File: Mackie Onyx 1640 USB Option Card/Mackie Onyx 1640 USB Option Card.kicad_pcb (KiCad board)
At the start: 2 copper layers, 193 x 90 mm, 7 parts, among them J1 Conn_02x17_Odd_Even, U1 XU316-1024-QF60B-C24, U2 CS5368-CQZ, U3 CS5368-CQZ, U4 CS5368-CQZ

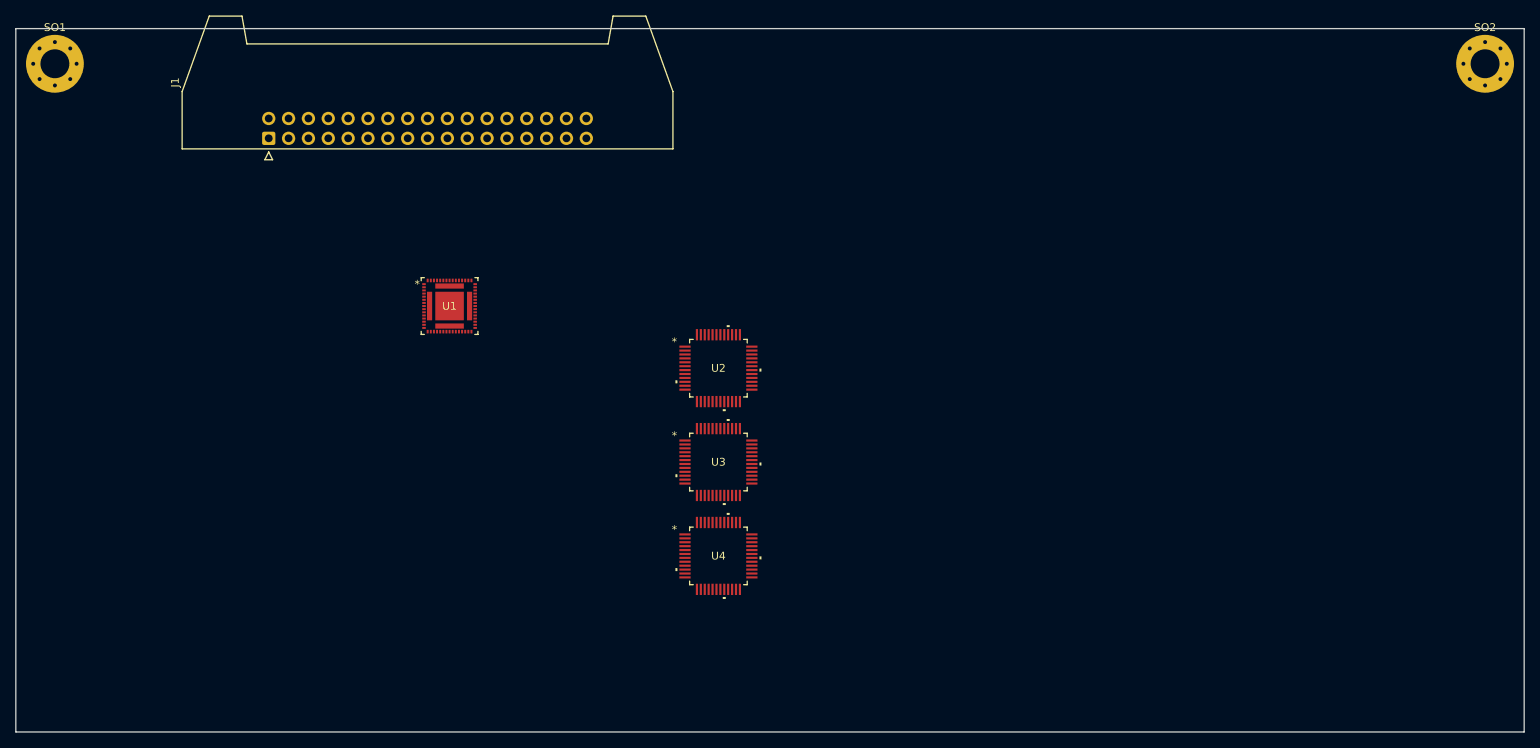
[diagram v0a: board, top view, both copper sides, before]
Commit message: Added a TI-TLV320 ADC Added power for ADC put the filter caps next to pins where they belong Added footprints for ADC and MCU
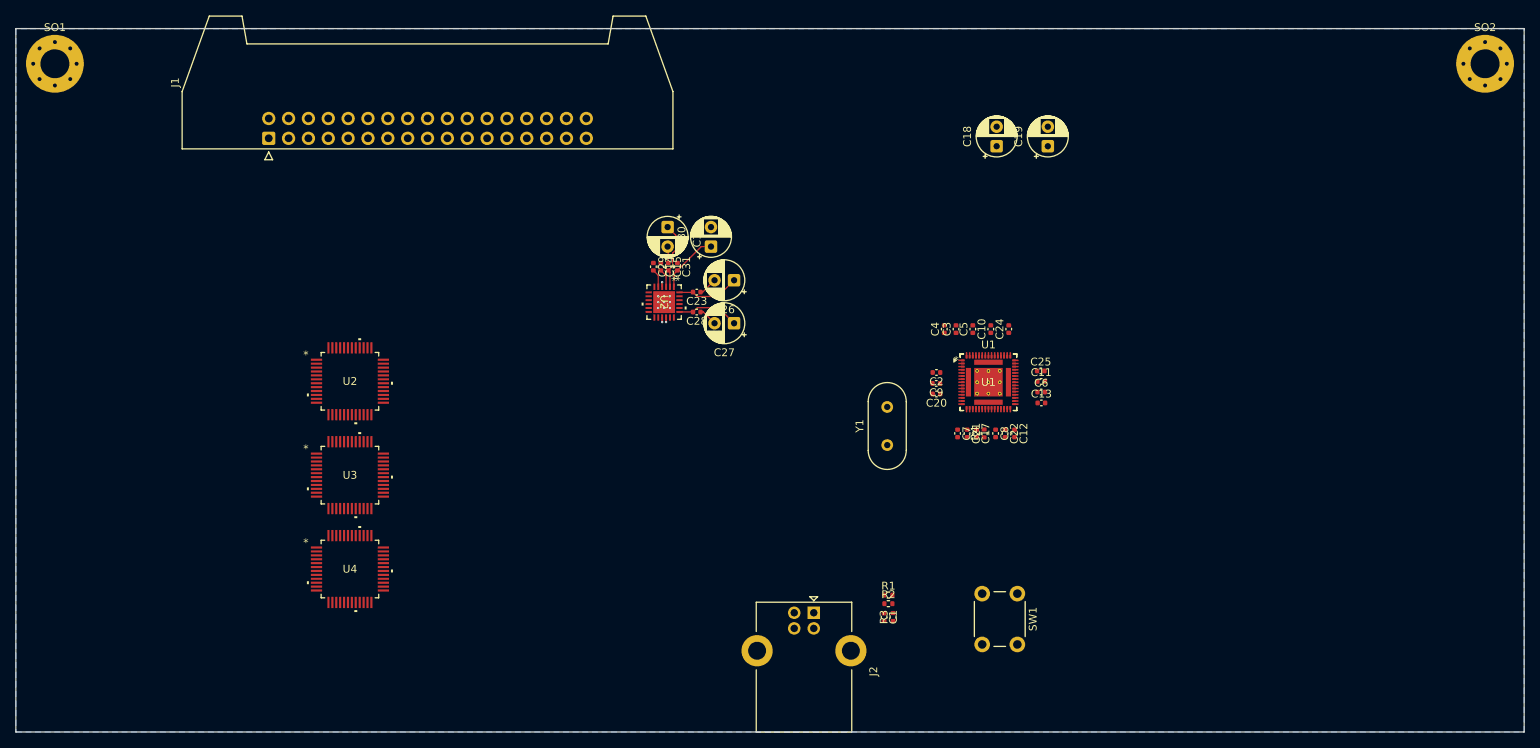
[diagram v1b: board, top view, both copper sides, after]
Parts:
- added C1: 2u2C, Capacitor_SMD:C_0402_1005Metric, F.Cu at (161.1, 125.3)
- added C10: 100nC, Capacitor_SMD:C_0402_1005Metric, F.Cu at (174.8, 88.5)
- added C11: 100nC, Capacitor_SMD:C_0402_1005Metric, F.Cu at (181.2, 95.2)
- added C12: 100nC, Capacitor_SMD:C_0402_1005Metric, F.Cu at (177.8, 101.8)
- added C13: 100nC, Capacitor_SMD:C_0402_1005Metric, F.Cu at (181.2, 97.9)
- added C14: 1uC, Capacitor_SMD:C_0402_1005Metric, F.Cu at (132.5, 80.5)
- added C15: 100nC, Capacitor_SMD:C_0402_1005Metric, F.Cu at (133.5, 80.5)
- added C16: 10uC_Polarized, Capacitor_THT:CP_Radial_D5.0mm_P2.50mm, F.Cu at (133.4, 75.4)
- added C17: 1uC, Capacitor_SMD:C_0402_1005Metric, F.Cu at (172.9, 101.8)
- added C18: 10uC_Polarized, Capacitor_THT:CP_Radial_D5.0mm_P2.50mm, F.Cu at (175.5, 65.0)
- added C19: 10uC_Polarized, Capacitor_THT:CP_Radial_D5.0mm_P2.50mm, F.Cu at (182.1, 65.0)
- added C2: 100nC, Capacitor_SMD:C_0402_1005Metric, F.Cu at (167.8, 94.0)
- added C20: 100nC, Capacitor_SMD:C_0402_1005Metric, F.Cu at (167.8, 96.8)
- added C21: 100nC, Capacitor_SMD:C_0402_1005Metric, F.Cu at (171.7, 101.8)
- added C22: 100nC, Capacitor_SMD:C_0402_1005Metric, F.Cu at (176.6, 101.8)
- added C23: 100nC, Capacitor_SMD:C_0402_1005Metric, F.Cu at (137.1, 83.7)
- added C24: 100nC, Capacitor_SMD:C_0402_1005Metric, F.Cu at (177.1, 88.5)
- added C25: 100nC, Capacitor_SMD:C_0402_1005Metric, F.Cu at (181.2, 93.8)
- added C26: 10uC_Polarized, Capacitor_THT:CP_Radial_D5.0mm_P2.50mm, F.Cu at (141.9, 82.2)
- added C27: 10uC_Polarized, Capacitor_THT:CP_Radial_D5.0mm_P2.50mm, F.Cu at (141.9, 87.7)
- added C28: 100nC, Capacitor_SMD:C_0402_1005Metric, F.Cu at (137.1, 86.3)
- added C29: 1uC, Capacitor_SMD:C_0402_1005Metric, F.Cu at (131.6, 80.5)
- added C3: 100nC, Capacitor_SMD:C_0402_1005Metric, F.Cu at (170.3, 88.5)
- added C30: 10uC_Polarized, Capacitor_THT:CP_Radial_D5.0mm_P2.50mm, F.Cu at (138.9, 77.9)
- added C31: 100nC, Capacitor_SMD:C_0402_1005Metric, F.Cu at (134.7, 80.5)
- added C4: 100nC, Capacitor_SMD:C_0402_1005Metric, F.Cu at (168.8, 88.5)
- added C5: 100nC, Capacitor_SMD:C_0402_1005Metric, F.Cu at (172.4, 88.5)
- added C6: 100nC, Capacitor_SMD:C_0402_1005Metric, F.Cu at (181.2, 96.5)
- added C7: 100nC, Capacitor_SMD:C_0402_1005Metric, F.Cu at (170.5, 101.8)
- added C8: 100nC, Capacitor_SMD:C_0402_1005Metric, F.Cu at (175.4, 101.8)
- added C9: 100nC, Capacitor_SMD:C_0402_1005Metric, F.Cu at (167.8, 95.4)
- added J2: USB_B, Connector_USB:USB_B_Lumberg_2411_02_Horizontal, F.Cu at (152.1, 124.7)
- added R1: 47kR, Resistor_SMD:R_0402_1005Metric, F.Cu at (161.7, 122.5)
- added R2: 220kR, Resistor_SMD:R_0402_1005Metric, F.Cu at (161.7, 123.6)
- added R3: 330kR, Resistor_SMD:R_0402_1005Metric, F.Cu at (162.2, 125.3)
- added R4: 600R@100Mhz, Resistor_SMD:R_0402_1005Metric, F.Cu at (173.9, 101.8)
- added SW1: SW_Push, Button_Switch_THT:SW_PUSH_6mm, F.Cu at (178.2, 122.3)
- added U1: XU316-1024-QF60B-C24, Package_DFN_QFN:QFN-60-1EP_7x7mm_P0.4mm_EP3.4x3.4mm_ThermalVias, F.Cu at (174.4, 95.2)
- added U2: TLV320ADC5140IRTWR, Mackie Onyx 1640 USB Option Card:RTW24_4P15X4P15_TEX, F.Cu at (132.9, 85.0)
- added Y1: 24MHz Crystal, Crystal:Crystal_HC49-U_Vertical, F.Cu at (161.5, 103.3)
- moved U1 69.6 mm to (174.4, 95.2)
- moved U2 47.2 mm to (92.8, 95.1)
- moved U3 47.2 mm to (92.8, 107.1)
- moved U4 47.2 mm to (92.8, 119.2)
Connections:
- J1 pad 1: unconnected-(J1-Pin_1-Pad1) -> /Connector/CH1
- J1 pad 10: unconnected-(J1-Pin_10-Pad10) -> /Connector/CH10
- J1 pad 11: unconnected-(J1-Pin_11-Pad11) -> /Connector/CH11
- J1 pad 12: unconnected-(J1-Pin_12-Pad12) -> /Connector/CH12
- J1 pad 13: unconnected-(J1-Pin_13-Pad13) -> /Connector/CH13
- J1 pad 14: unconnected-(J1-Pin_14-Pad14) -> /Connector/CH14
- J1 pad 15: unconnected-(J1-Pin_15-Pad15) -> /Connector/CH15
- J1 pad 16: unconnected-(J1-Pin_16-Pad16) -> /Connector/CH16
- J1 pad 17: unconnected-(J1-Pin_17-Pad17) -> GND
- J1 pad 18: unconnected-(J1-Pin_18-Pad18) -> GND
- J1 pad 19: unconnected-(J1-Pin_19-Pad19) -> /Connector/L_SEND
- J1 pad 2: unconnected-(J1-Pin_2-Pad2) -> /Connector/CH2
- J1 pad 20: unconnected-(J1-Pin_20-Pad20) -> /Connector/R_SEND
- J1 pad 21: unconnected-(J1-Pin_21-Pad21) -> GND
- J1 pad 22: unconnected-(J1-Pin_22-Pad22) -> GND
- J1 pad 23: unconnected-(J1-Pin_23-Pad23) -> /Connector/L_IN
- J1 pad 24: unconnected-(J1-Pin_24-Pad24) -> /Connector/R_IN
- J1 pad 25: unconnected-(J1-Pin_25-Pad25) -> +15V
- J1 pad 26: unconnected-(J1-Pin_26-Pad26) -> +15V
- J1 pad 27: unconnected-(J1-Pin_27-Pad27) -> -15V
- J1 pad 28: unconnected-(J1-Pin_28-Pad28) -> -15V
- J1 pad 29: unconnected-(J1-Pin_29-Pad29) -> Earth
- J1 pad 3: unconnected-(J1-Pin_3-Pad3) -> /Connector/CH3
- J1 pad 30: unconnected-(J1-Pin_30-Pad30) -> Earth
- J1 pad 31: unconnected-(J1-Pin_31-Pad31) -> Earth
- J1 pad 32: unconnected-(J1-Pin_32-Pad32) -> +5V
- J1 pad 33: unconnected-(J1-Pin_33-Pad33) -> +5V
- J1 pad 34: unconnected-(J1-Pin_34-Pad34) -> +5V
- J1 pad 4: unconnected-(J1-Pin_4-Pad4) -> /Connector/CH4
- J1 pad 5: unconnected-(J1-Pin_5-Pad5) -> /Connector/CH5
- J1 pad 6: unconnected-(J1-Pin_6-Pad6) -> /Connector/CH6
- J1 pad 7: unconnected-(J1-Pin_7-Pad7) -> /Connector/CH7
- J1 pad 8: unconnected-(J1-Pin_8-Pad8) -> /Connector/CH8
- J1 pad 9: unconnected-(J1-Pin_9-Pad9) -> /Connector/CH9
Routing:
- net ADV1_AVDD: track 0.00 -> 15.9 mm
- net GND: track 0.00 -> 8.69 mm, vias 0 -> 12
- net ADV1_AREG: track 0.00 -> 8.57 mm
- net ADV1_DREG: track 0.00 -> 8.09 mm
- net ADV1_VREF: track 0.00 -> 2.36 mm
- net ADV1_MICBIAS: track 0.00 -> 2.34 mm
- added copper zone on B.Cu, net GND

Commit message: Added Balancing Circuit ADC input is balanced, card connector isnt schematic following the one from original firewire card since ADC input voltage ratings are very close quad-op-amp-ic is placeholder with standard footprint, a higher quality one may be used on BOM did a bit of more or less rough PCB layouting
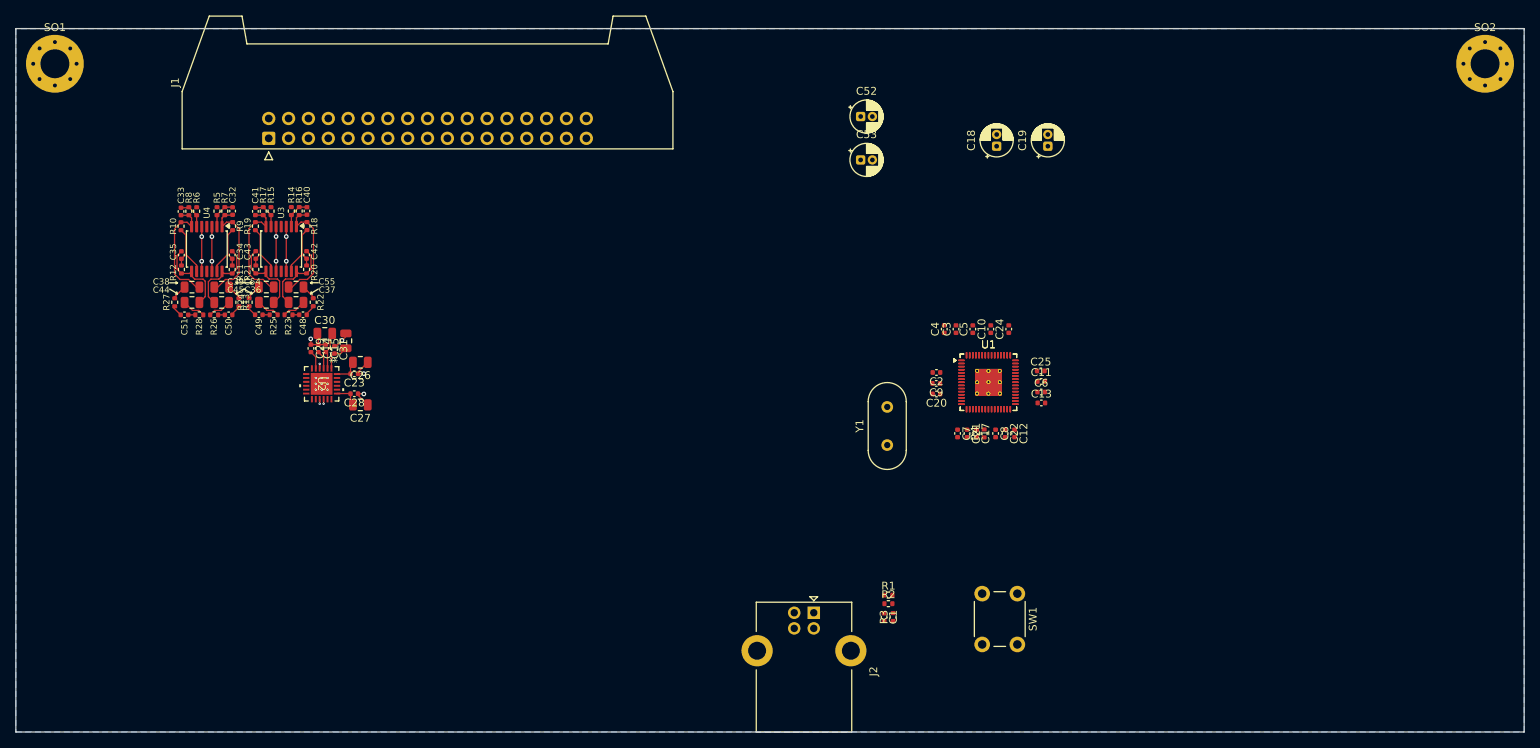
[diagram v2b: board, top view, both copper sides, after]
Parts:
- removed the U2 at (92.8, 95.1)
- added C32: 100pC, Capacitor_SMD:C_0402_1005Metric, F.Cu at (77.7, 73.3)
- added C33: 100pC, Capacitor_SMD:C_0402_1005Metric, F.Cu at (71.1, 73.4)
- added C34: 100pC, Capacitor_SMD:C_0402_1005Metric, F.Cu at (77.7, 79.0)
- added C35: 100pC, Capacitor_SMD:C_0402_1005Metric, F.Cu at (71.2, 79.0)
- added C36: 10uC, Capacitor_SMD:C_0805_2012Metric, F.Cu at (76.3, 85.0)
- added C37: 10uC, Capacitor_SMD:C_0805_2012Metric, F.Cu at (85.9, 85.0)
- added C38: 10uC, Capacitor_SMD:C_0805_2012Metric, F.Cu at (72.5, 83.1)
- added C39: 10uC, Capacitor_SMD:C_0805_2012Metric, F.Cu at (82.1, 83.1)
- added C40: 100pC, Capacitor_SMD:C_0402_1005Metric, F.Cu at (87.3, 73.3)
- added C41: 100pC, Capacitor_SMD:C_0402_1005Metric, F.Cu at (80.7, 73.4)
- added C42: 100pC, Capacitor_SMD:C_0402_1005Metric, F.Cu at (87.2, 79.0)
- added C43: 100pC, Capacitor_SMD:C_0402_1005Metric, F.Cu at (80.7, 79.0)
- added C44: 10uC, Capacitor_SMD:C_0805_2012Metric, F.Cu at (72.5, 85.0)
- added C45: 10uC, Capacitor_SMD:C_0805_2012Metric, F.Cu at (82.1, 85.0)
- added C48: 1n5C, Capacitor_SMD:C_0402_1005Metric, F.Cu at (86.7, 86.6)
- added C49: 1n5C, Capacitor_SMD:C_0402_1005Metric, F.Cu at (81.1, 86.6)
- added C50: 1n5C, Capacitor_SMD:C_0402_1005Metric, F.Cu at (77.2, 86.6)
- added C51: 1n5C, Capacitor_SMD:C_0402_1005Metric, F.Cu at (71.6, 86.6)
- added C52: 10uC_Polarized, Capacitor_THT:CP_Radial_D4.0mm_P1.50mm, F.Cu at (158.1, 61.2)
- added C53: 10uC_Polarized, Capacitor_THT:CP_Radial_D4.0mm_P1.50mm, F.Cu at (158.1, 66.8)
- added C54: 10uC, Capacitor_SMD:C_0805_2012Metric, F.Cu at (76.3, 83.1)
- added C55: 10uC, Capacitor_SMD:C_0805_2012Metric, F.Cu at (85.9, 83.1)
- added R10: 4k7R, Resistor_SMD:R_0402_1005Metric, F.Cu at (71.1, 75.3)
- added R11: 4k7R, Resistor_SMD:R_0402_1005Metric, F.Cu at (77.7, 80.8)
- added R12: 4k7R, Resistor_SMD:R_0402_1005Metric, F.Cu at (71.2, 80.8)
- added R13: 330R, Resistor_SMD:R_0402_1005Metric, F.Cu at (78.5, 85.0)
- added R14: 20kR, Resistor_SMD:R_0402_1005Metric, F.Cu at (85.3, 73.3)
- added R15: 20kR, Resistor_SMD:R_0402_1005Metric, F.Cu at (82.7, 73.4)
- added R16: 2k2R, Resistor_SMD:R_0402_1005Metric, F.Cu at (86.3, 73.3)
- added R17: 2k2R, Resistor_SMD:R_0402_1005Metric, F.Cu at (81.7, 73.4)
- added R18: 4k7R, Resistor_SMD:R_0402_1005Metric, F.Cu at (87.3, 75.3)
- added R19: 4k7R, Resistor_SMD:R_0402_1005Metric, F.Cu at (80.7, 75.3)
- added R20: 4k7R, Resistor_SMD:R_0402_1005Metric, F.Cu at (87.2, 80.8)
- added R21: 4k7R, Resistor_SMD:R_0402_1005Metric, F.Cu at (80.7, 80.8)
- added R22: 330R, Resistor_SMD:R_0402_1005Metric, F.Cu at (88.1, 85.0)
- added R23: 330R, Resistor_SMD:R_0402_1005Metric, F.Cu at (84.9, 86.6)
- added R24: 330R, Resistor_SMD:R_0402_1005Metric, F.Cu at (79.8, 85.0)
- added R25: 330R, Resistor_SMD:R_0402_1005Metric, F.Cu at (83.0, 86.6)
- added R26: 330R, Resistor_SMD:R_0402_1005Metric, F.Cu at (75.4, 86.6)
- added R27: 330R, Resistor_SMD:R_0402_1005Metric, F.Cu at (70.3, 85.0)
- added R28: 330R, Resistor_SMD:R_0402_1005Metric, F.Cu at (73.5, 86.6)
- added R5: 20kR, Resistor_SMD:R_0402_1005Metric, F.Cu at (75.7, 73.4)
- added R6: 20kR, Resistor_SMD:R_0402_1005Metric, F.Cu at (73.1, 73.4)
- added R7: 2k2R, Resistor_SMD:R_0402_1005Metric, F.Cu at (76.7, 73.4)
- added R8: 2k2R, Resistor_SMD:R_0402_1005Metric, F.Cu at (72.1, 73.4)
- added R9: 4k7R, Resistor_SMD:R_0402_1005Metric, F.Cu at (77.7, 75.3)
- C16, C26, C27, C30: value 10uC_Polarized -> 10uC; footprint Capacitor_THT:CP_Radial_D5.0mm_P2.50mm -> Capacitor_SMD:C_0805_2012Metric
- C18, C19: footprint Capacitor_THT:CP_Radial_D5.0mm_P2.50mm -> Capacitor_THT:CP_Radial_D4.0mm_P1.50mm
- U1: footprint xmox:QFN_F60B-C24_XMO -> Package_DFN_QFN:QFN-60-1EP_7x7mm_P0.4mm_EP3.4x3.4mm_ThermalVias
- U3, U4: value CS5368-CQZ -> LM2902; footprint adc:CIR-LQFP-48 -> Package_SO:TSSOP-14_4.4x5mm_P0.65mm
- moved C30 50.7 mm to (89.5, 89.0), turned to 0 degrees
- moved C26 49.0 mm to (94.1, 92.7)
- moved C27 49.0 mm to (94.1, 98.2)
- moved C31 45.1 mm to (90.8, 91.1)
- moved C14 45.0 mm to (88.7, 90.9)
- moved C23 45.0 mm to (93.3, 94.2)
- moved C28 45.0 mm to (93.3, 96.7)
- moved C15 45.0 mm to (89.7, 90.9)
- moved C29 45.0 mm to (87.8, 90.9)
- moved U2 45.0 mm to (89.1, 95.5)
- moved U4 44.9 mm to (74.4, 78.2), turned to -90 degrees
- moved C16 43.7 mm to (92.2, 90.0)
- moved U3 30.2 mm to (84.0, 78.2), turned to -90 degrees
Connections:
- C16 pad 1: ADV1_AREG -> GND
- C16 pad 2: GND -> ADV1_AVDD
- C26 pad 1: ADV1_DREG -> GND
- C26 pad 2: GND -> ADV1_DREG
- C27 pad 1: ADV1_AVDD -> GND
- C27 pad 2: GND -> ADV1_AVDD
- C30 pad 1: ADV1_AVDD -> GND
- C30 pad 2: GND -> ADV1_AREG
- J1 pad 1: /Connector/CH1 -> /ADC/IN1
- J1 pad 2: /Connector/CH2 -> /ADC/IN2
- J1 pad 25: +15V -> BAL_V+
- J1 pad 26: +15V -> BAL_V+
- J1 pad 27: -15V -> BAL_V-
- J1 pad 28: -15V -> BAL_V-
- J1 pad 3: /Connector/CH3 -> /ADC/IN3
- J1 pad 4: /Connector/CH4 -> /ADC/IN4
- U1 pad 12: unconnected-(U1-VDD-Pad12) -> MCU_VDD1
- U1 pad 15: unconnected-(U1-XOUT-Pad15) -> Net-(U1-XOUT)
- U1 pad 16: unconnected-(U1-XIN-Pad16) -> Net-(U1-XIN)
- U1 pad 17: unconnected-(U1-VDDIOB18-Pad17) -> MCU_USB_VDD1V8
- U1 pad 19: unconnected-(U1-VDD-Pad19) -> MCU_VDD1
- U1 pad 21: unconnected-(U1-RST_N-Pad21) -> Net-(U1-RST_N)
- U1 pad 22: unconnected-(U1-PLL_AVDD-Pad22) -> MCU_PLL_AVDD
- U1 pad 26: unconnected-(U1-VDDIOB18-Pad26) -> MCU_USB_VDD1V8
- U1 pad 27: unconnected-(U1-VDD-Pad27) -> MCU_VDD1
- U1 pad 28: unconnected-(U1-USB_DM-Pad28) -> /USB Connector/D-
- U1 pad 29: unconnected-(U1-USB_DP-Pad29) -> /USB Connector/D+
- U1 pad 30: unconnected-(U1-USB_VDD33-Pad30) -> ADV1_AVDD
- U1 pad 31: unconnected-(U1-USB_VDD18-Pad31) -> MCU_USB_VDD1V8
- U1 pad 34: unconnected-(U1-VDD-Pad34) -> MCU_VDD1
- U1 pad 38: unconnected-(U1-VDDIOR-Pad38) -> ADV1_AVDD
- U1 pad 4: unconnected-(U1-VDD-Pad4) -> MCU_VDD1
- U1 pad 42: unconnected-(U1-VDD-Pad42) -> MCU_VDD1
- U1 pad 49: unconnected-(U1-VDD-Pad49) -> MCU_VDD1
- U1 pad 52: unconnected-(U1-VDDIOT-Pad52) -> ADV1_AVDD
- U1 pad 57: unconnected-(U1-VDD-Pad57) -> MCU_VDD1
- U1 pad 61: unconnected-(U1-VDD-Pad61) -> MCU_VDD1
- U1 pad 8: unconnected-(U1-VDDIOL-Pad8) -> ADV1_AVDD
- U2 pad 10: unconnected-(U2-IN3P_GPI3-Pad10) -> /ADC/2CH_electronic-balancer-2/1+
- U2 pad 11: unconnected-(U2-IN3M_GPO3-Pad11) -> /ADC/2CH_electronic-balancer-2/1-
- U2 pad 12: unconnected-(U2-IN4P_GPI4-Pad12) -> /ADC/2CH_electronic-balancer-2/2+
- U2 pad 13: unconnected-(U2-IN4M_GPO4-Pad13) -> /ADC/2CH_electronic-balancer-2/2-
- U2 pad 6: unconnected-(U2-IN1P_GPI1-Pad6) -> /ADC/2CH_electronic-balancer-1/1+
- U2 pad 7: unconnected-(U2-IN1M_GPO1-Pad7) -> /ADC/2CH_electronic-balancer-1/1-
- U2 pad 8: unconnected-(U2-IN2P_GPI2-Pad8) -> /ADC/2CH_electronic-balancer-1/2+
- U2 pad 9: unconnected-(U2-IN2M_GPO2-Pad9) -> /ADC/2CH_electronic-balancer-1/2-
- U3 pad 1: unconnected-(U3-AIN2+-Pad1) -> Net-(C40-Pad1)
- U3 pad 10: unconnected-(U3-GND-Pad10) -> GND
- U3 pad 11: unconnected-(U3-AIN4+-Pad11) -> BAL_V-
- U3 pad 12: unconnected-(U3-AIN4--Pad12) -> GND
- U3 pad 13: unconnected-(U3-AIN3+-Pad13) -> Net-(U3D--)
- U3 pad 14: unconnected-(U3-AIN3--Pad14) -> Net-(C37-Pad1)
- U3 pad 2: unconnected-(U3-AIN2--Pad2) -> Net-(U3A--)
- U3 pad 3: unconnected-(U3-GND-Pad3) -> GND
- U3 pad 4: unconnected-(U3-VA-Pad4) -> BAL_V+
- U3 pad 5: unconnected-(U3-REF_GND-Pad5) -> GND
- U3 pad 6: unconnected-(U3-FILT+-Pad6) -> Net-(U3B--)
- U3 pad 7: unconnected-(U3-VQ-Pad7) -> Net-(C39-Pad1)
- U3 pad 8: unconnected-(U3-GND-Pad8) -> Net-(C43-Pad1)
- U3 pad 9: unconnected-(U3-VA-Pad9) -> Net-(U3C--)
- U4 pad 1: unconnected-(U4-AIN2+-Pad1) -> Net-(C32-Pad1)
- U4 pad 10: unconnected-(U4-GND-Pad10) -> GND
- U4 pad 11: unconnected-(U4-AIN4+-Pad11) -> BAL_V-
- U4 pad 12: unconnected-(U4-AIN4--Pad12) -> GND
- U4 pad 13: unconnected-(U4-AIN3+-Pad13) -> Net-(U4D--)
- U4 pad 14: unconnected-(U4-AIN3--Pad14) -> Net-(C34-Pad1)
- U4 pad 2: unconnected-(U4-AIN2--Pad2) -> Net-(U4A--)
- U4 pad 3: unconnected-(U4-GND-Pad3) -> GND
- U4 pad 4: unconnected-(U4-VA-Pad4) -> BAL_V+
- U4 pad 5: unconnected-(U4-REF_GND-Pad5) -> GND
- U4 pad 6: unconnected-(U4-FILT+-Pad6) -> Net-(U4B--)
- U4 pad 7: unconnected-(U4-VQ-Pad7) -> Net-(C33-Pad1)
- U4 pad 8: unconnected-(U4-GND-Pad8) -> Net-(C35-Pad1)
- U4 pad 9: unconnected-(U4-VA-Pad9) -> Net-(U4C--)
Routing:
- net GND: track 8.69 -> 36.7 mm, vias 12 -> 24
- net Net-(C33-Pad1): track 0.00 -> 15.0 mm
- net Net-(C39-Pad1): track 0.00 -> 15.0 mm
- net Net-(C32-Pad1): track 0.00 -> 15.0 mm
- net Net-(C40-Pad1): track 0.00 -> 15.0 mm
- net Net-(C43-Pad1): track 0.00 -> 10.4 mm
- net Net-(C35-Pad1): track 0.00 -> 10.4 mm
- net Net-(C34-Pad1): track 0.00 -> 10.3 mm
- net Net-(C37-Pad1): track 0.00 -> 10.3 mm
- net ADV1_AVDD: track 15.9 -> 7.30 mm
- net Net-(U3D--): track 0.00 -> 7.77 mm
- net Net-(U4D--): track 0.00 -> 7.77 mm
- net Net-(U4C--): track 0.00 -> 7.75 mm
- net Net-(U3C--): track 0.00 -> 7.75 mm
- net ADV1_DREG: track 8.09 -> 3.33 mm
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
